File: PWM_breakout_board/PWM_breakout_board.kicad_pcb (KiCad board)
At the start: 2 copper layers, 130 x 40 mm, 8 parts, among them J1 Power, J2 Input, J3 Out 1, J4 Out 2, J5 Out 3, J6 Out 4

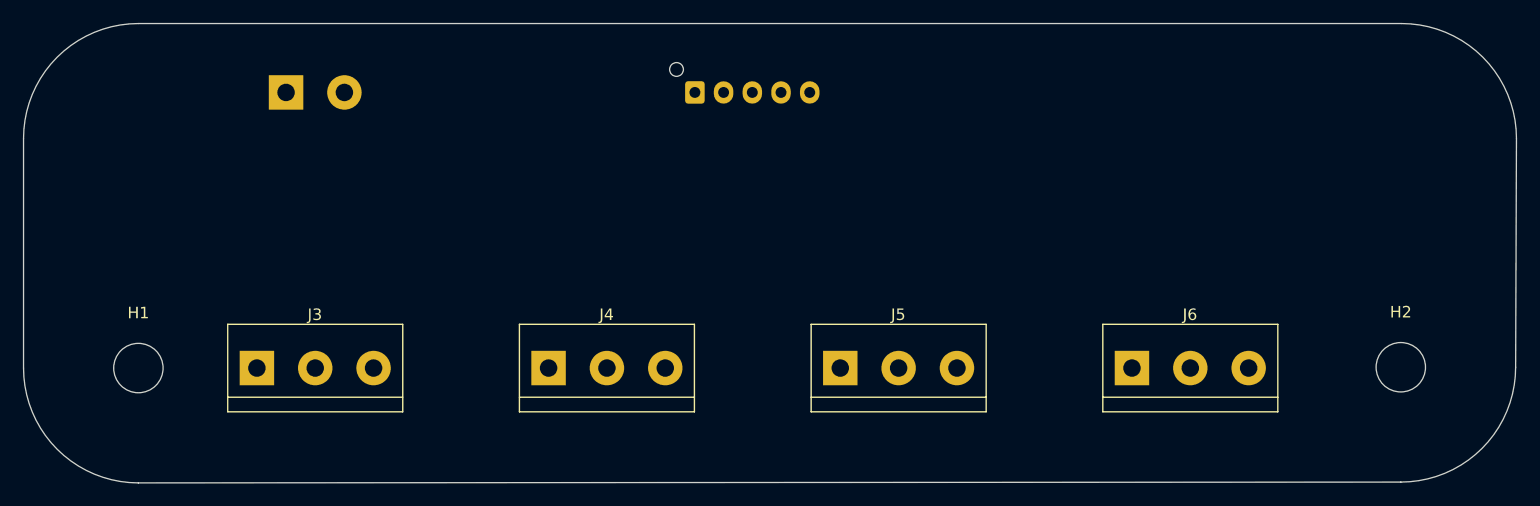
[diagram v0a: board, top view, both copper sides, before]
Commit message: Roughly routes PWM breakout board as a first draft
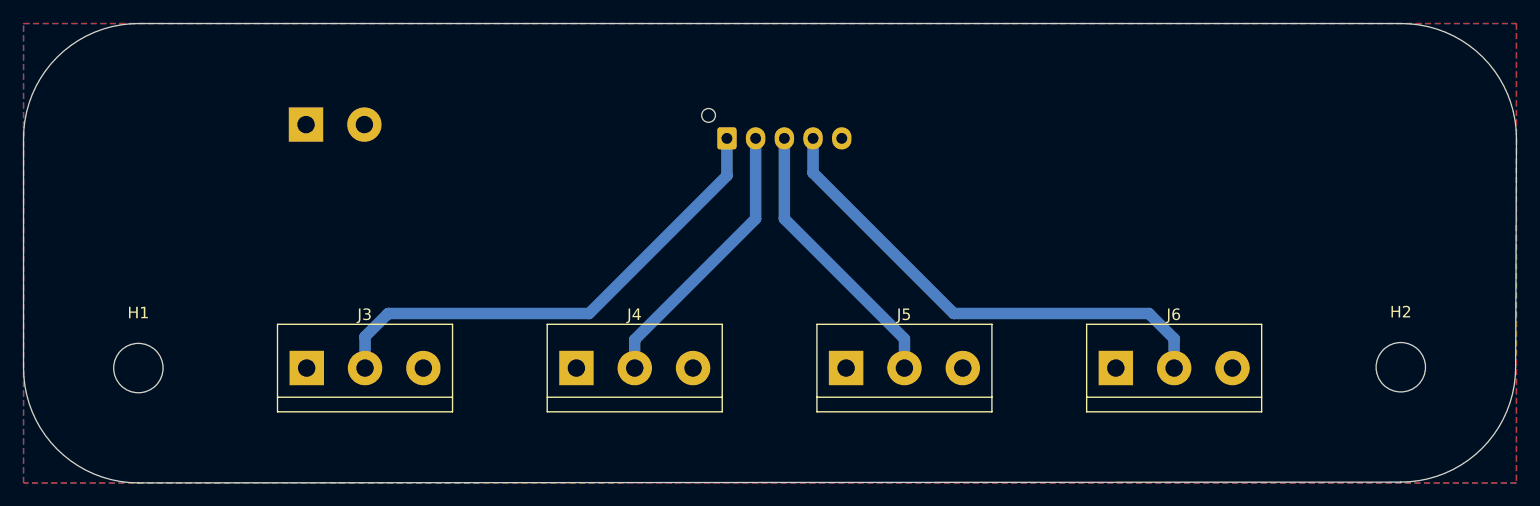
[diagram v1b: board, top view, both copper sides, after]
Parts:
- moved J2 4.88 mm to (141.2, 80.0)
- moved J3 4.34 mm to (104.7, 100.0)
- moved J1 3.30 mm to (104.6, 78.8)
- moved J4 2.42 mm to (128.1, 100.0)
- moved J6 1.41 mm to (175.1, 100.0)
- moved J5 0.51 mm to (151.6, 100.0)
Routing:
- net SIG1: track 0.00 -> 43.3 mm
- net SIG4: track 0.00 -> 43.0 mm
- net SIG2: track 0.00 -> 24.4 mm
- net SIG3: track 0.00 -> 24.3 mm
- added copper zone on F.Cu, net GND
- added copper zone on B.Cu, net VCC
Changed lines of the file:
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@@
   )
   (setup
+    (stackup
+      (layer "F.SilkS" (type "Top Silk Screen"))
+      (layer "F.Paste" (type "Top Solder Paste"))
+      (layer "F.Mask" (type "Top Solder Mask") (thickness 0.01))
+      (layer "F.Cu" (type "copper") (thickness 0.035))
+      (layer "dielectric 1" (type "core") (thickness 1.51) (material "FR4") (epsilon_r 4.5) (loss_tangent 0.02))
+      (layer "B.Cu" (type "copper") (thickness 0.035))
+      (layer "B.Mask" (type "Bottom Solder Mask") (thickness 0.01))
+      (layer "B.Paste" (type "Bottom Solder Paste"))
+      (layer "B.SilkS" (type "Bottom Silk Screen"))
+      (copper_finish "None")
+      (dielectric_constraints no)
+    )
     (pad_to_mask_clearance 0)
     (pcbplotparams
@@
   (net 6 "SIG4")
   (footprint "TerminalBlock:TerminalBlock_bornier-3_P5.08mm" (layer "F.Cu")
-    (at 151.12 100)
+    (at 151.627358 100)
     (descr "simple 3-pin terminal block, pitch 5.08mm, revamped version of bornier3")
     (tags "terminal block bornier3")
@@
   )
   (footprint "TerminalBlock:TerminalBlock_bornier-3_P5.08mm" (layer "F.Cu")
-    (at 125.72 100)
+    (at 128.141572 100)
     (descr "simple 3-pin terminal block, pitch 5.08mm, revamped version of bornier3")
     (tags "terminal block bornier3")
@@
   )
   (footprint "TerminalBlock:TerminalBlock_bornier-3_P5.08mm" (layer "F.Cu")
-    (at 176.52 100)
+    (at 175.113144 100)
     (descr "simple 3-pin terminal block, pitch 5.08mm, revamped version of bornier3")
     (tags "terminal block bornier3")
@@
   )
   (footprint "TerminalBlock:TerminalBlock_bornier-3_P5.08mm" (layer "F.Cu")
-    (at 100.32 100)
+    (at 104.655786 100)
     (descr "simple 3-pin terminal block, pitch 5.08mm, revamped version of bornier3")
     (tags "terminal block bornier3")
@@
   )
   (footprint "Connector_JST:JST_XH_B5B-XH-AM_1x05_P2.50mm_Vertical" (layer "B.Cu")
-    (at 138.46 76)
+    (at 141.25 80)
     (descr "JST XH series connector, B5B-XH-AM, with boss (http://www.jst-mfg.com/product/pdf/eng/eXH.pdf), generated with kicad-footprint-generator")
     (tags "connector JST XH vertical boss")
@@
   )
   (footprint "TerminalBlock:TerminalBlock_bornier-2_P5.08mm" (layer "B.Cu")
-    (at 102.86 76)
+    (at 104.6 78.8)
     (descr "simple 2-pin terminal block, pitch 5.08mm, revamped version of bornier2")
     (tags "terminal block bornier2")
@@
     )
   )
-  (gr_line (start 209.928932 99.928932) (end 210 80)
-    (stroke (width 0.1) (type default)) (layer "Edge.Cuts"))
-  (gr_arc (start 90 110) (mid 82.928932 107.071068) (end 80 100)
-    (stroke (width 0.1) (type default)) (layer "Edge.Cuts"))
-  (gr_line (start 90 110) (end 199.928932 109.928932)
-    (stroke (width 0.1) (type default)) (layer "Edge.Cuts"))
-  (gr_line (start 80 80) (end 80 100)
-    (stroke (width 0.1) (type default)) (layer "Edge.Cuts"))
-  (gr_arc (start 200 70) (mid 207.071068 72.928932) (end 210 80)
-    (stroke (width 0.1) (type default)) (layer "Edge.Cuts"))
-  (gr_line (start 90 70) (end 200 70)
-    (stroke (width 0.1) (type default)) (layer "Edge.Cuts"))
-  (gr_arc (start 209.928932 99.928932) (mid 207 107) (end 199.928932 109.928932)
-    (stroke (width 0.1) (type default)) (layer "Edge.Cuts"))
-  (gr_arc (start 80 80) (mid 82.928932 72.928932) (end 90 70)
-    (stroke (width 0.1) (type default)) (layer "Edge.Cuts"))
+  (gr_line locked (start 209.928932 99.928932) (end 210 80)
+    (stroke (width 0.1) (type default)) (layer "Edge.Cuts"))
+  (gr_arc locked (start 90 110) (mid 82.928932 107.071068) (end 80 100)
+    (stroke (width 0.1) (type default)) (layer "Edge.Cuts"))
+  (gr_line locked (start 90 110) (end 199.928932 109.928932)
+    (stroke (width 0.1) (type default)) (layer "Edge.Cuts"))
+  (gr_line locked (start 80 80) (end 80 100)
+    (stroke (width 0.1) (type default)) (layer "Edge.Cuts"))
+  (gr_arc locked (start 200 70) (mid 207.071068 72.928932) (end 210 80)
+    (stroke (width 0.1) (type default)) (layer "Edge.Cuts"))
+  (gr_line locked (start 90 70) (end 200 70)
+    (stroke (width 0.1) (type default)) (layer "Edge.Cuts"))
+  (gr_arc locked (start 209.928932 99.928932) (mid 207 107) (end 199.928932 109.928932)
+    (stroke (width 0.1) (type default)) (layer "Edge.Cuts"))
+  (gr_arc locked (start 80 80) (mid 82.928932 72.928932) (end 90 70)
+    (stroke (width 0.1) (type default)) (layer "Edge.Cuts"))
+  (segment (start 141.25 80) (end 141.25 83.25) (width 1) (layer "B.Cu") (net 3))
+  (segment (start 111.75 95.25) (end 109.735786 97.264214) (width 1) (layer "B.Cu") (net 3))
+  (segment (start 129.25 95.25) (end 111.75 95.25) (width 1) (layer "B.Cu") (net 3))
+  (segment (start 109.735786 97.264214) (end 109.735786 100) (width 1) (layer "B.Cu") (net 3))
+  (segment (start 141.25 83.25) (end 129.25 95.25) (width 1) (layer "B.Cu") (net 3))
+  (segment (start 143.75 80) (end 143.75 87) (width 1) (layer "B.Cu") (net 4))
+  (segment (start 133.221572 97.528428) (end 133.221572 100) (width 1) (layer "B.Cu") (net 4))
+  (segment (start 143.75 87) (end 133.221572 97.528428) (width 1) (layer "B.Cu") (net 4))
+  (segment (start 146.25 80) (end 146.25 87) (width 1) (layer "B.Cu") (net 5))
+  (segment (start 156.707358 97.457358) (end 156.707358 100) (width 1) (layer "B.Cu") (net 5))
+  (segment (start 146.25 87) (end 156.707358 97.457358) (width 1) (layer "B.Cu") (net 5))
+  (segment (start 180.193144 97.443144) (end 180.193144 100) (width 1) (layer "B.Cu") (net 6))
+  (segment (start 178 95.25) (end 180.193144 97.443144) (width 1) (layer "B.Cu") (net 6))
+  (segment (start 148.75 83) (end 161 95.25) (width 1) (layer "B.Cu") (net 6))
+  (segment (start 161 95.25) (end 178 95.25) (width 1) (layer "B.Cu") (net 6))
+  (segment (start 148.75 80) (end 148.75 83) (width 1) (layer "B.Cu") (net 6))
+  (zone (net 2) (net_name "GND") (layer "F.Cu") (hatch edge 0.5)
+    (connect_pads (clearance 0.5))
+    (min_thickness 0.25) (filled_areas_thickness no)
+    (fill yes (thermal_gap 0.5) (thermal_bridge_width 0.5))
+    (polygon
+      (pts
+        (xy 80 70)
+        (xy 210 70)
+        (xy 210 110)
+        (xy 80 110)
+      )
+    )
+  )
+  (zone (net 1) (net_name "VCC") (layer "B.Cu") (hatch edge 0.5)
+    (priority 1)
+    (connect_pads (clearance 0.5))
+    (min_thickness 0.25) (filled_areas_thickness no)
+    (fill yes (thermal_gap 0.5) (thermal_bridge_width 0.5))
+    (polygon
+      (pts
+        (xy 80 70)
+        (xy 210 70)
+        (xy 210 110)
+        (xy 80 110)
+      )
+    )
+  )
 )

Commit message: add personal logo + infos into main board, edited F.silk labels into main board, changed dimensions of daughter board + reposition of components, included logo .pretty into project.
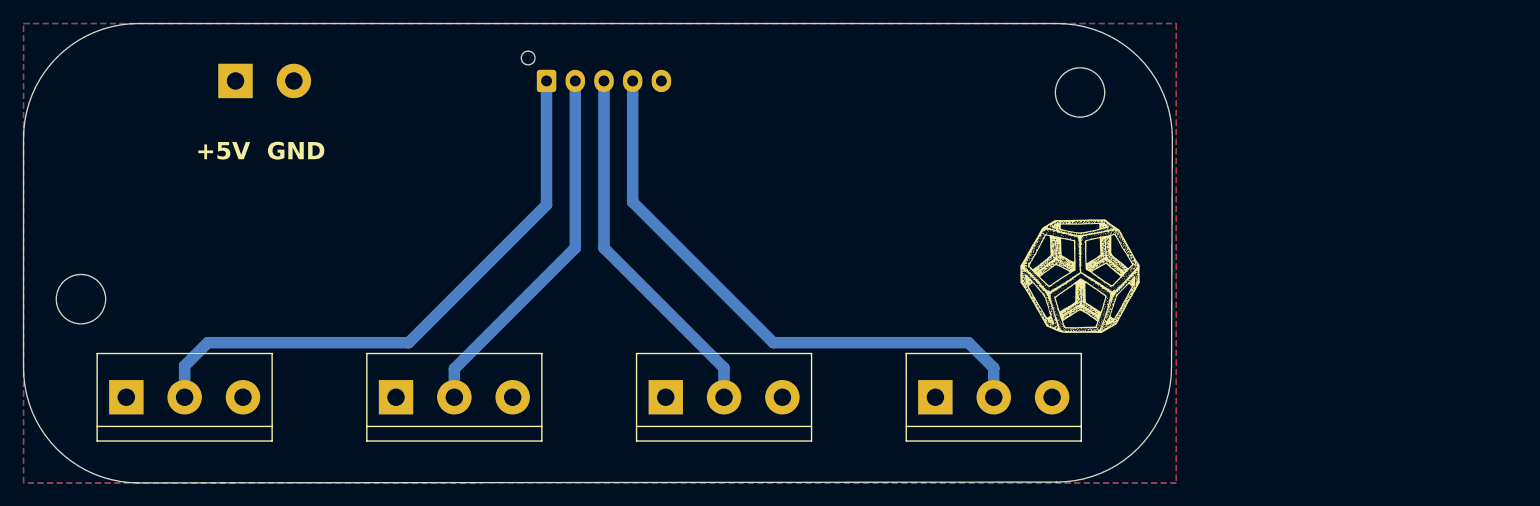
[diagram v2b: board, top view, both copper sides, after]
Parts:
- added G***: LOGO, MatheusLibs:mnds_logo_normal, F.Cu at (172.0, 92.0)
- moved H2 115.1 mm to (85.0, 94.0)
- moved H1 85.4 mm to (172.0, 76.0)
- moved J2 16.5 mm to (125.5, 75.0)
- moved J3 15.9 mm to (88.9, 102.5)
- moved J4 15.9 mm to (112.4, 102.5)
- moved J5 15.9 mm to (135.9, 102.5)
- moved J6 15.9 mm to (159.4, 102.5)
- moved J1 7.22 mm to (98.5, 75.0)
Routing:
- net SIG2: track 24.4 -> 31.9 mm
- net SIG4: track 43.0 -> 50.5 mm
- net SIG3: track 24.3 -> 31.9 mm
- net SIG1: track 43.3 -> 50.8 mm
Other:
- board size 130 x 40 mm -> 100 x 40 mm
- board text added: "+5V GND"
- board text added: "DMX SERVO SPLITTER rev a - 2023 DELED - AMIEIRO"
